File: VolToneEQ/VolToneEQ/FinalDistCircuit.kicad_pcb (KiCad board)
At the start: 4 copper layers, 96.8 x 83.6 mm, 93 parts, among them Q1 ZTX951, Q2 ZTX951, U1 TL072, U2 TL072, U3 TL072, U4 TL072

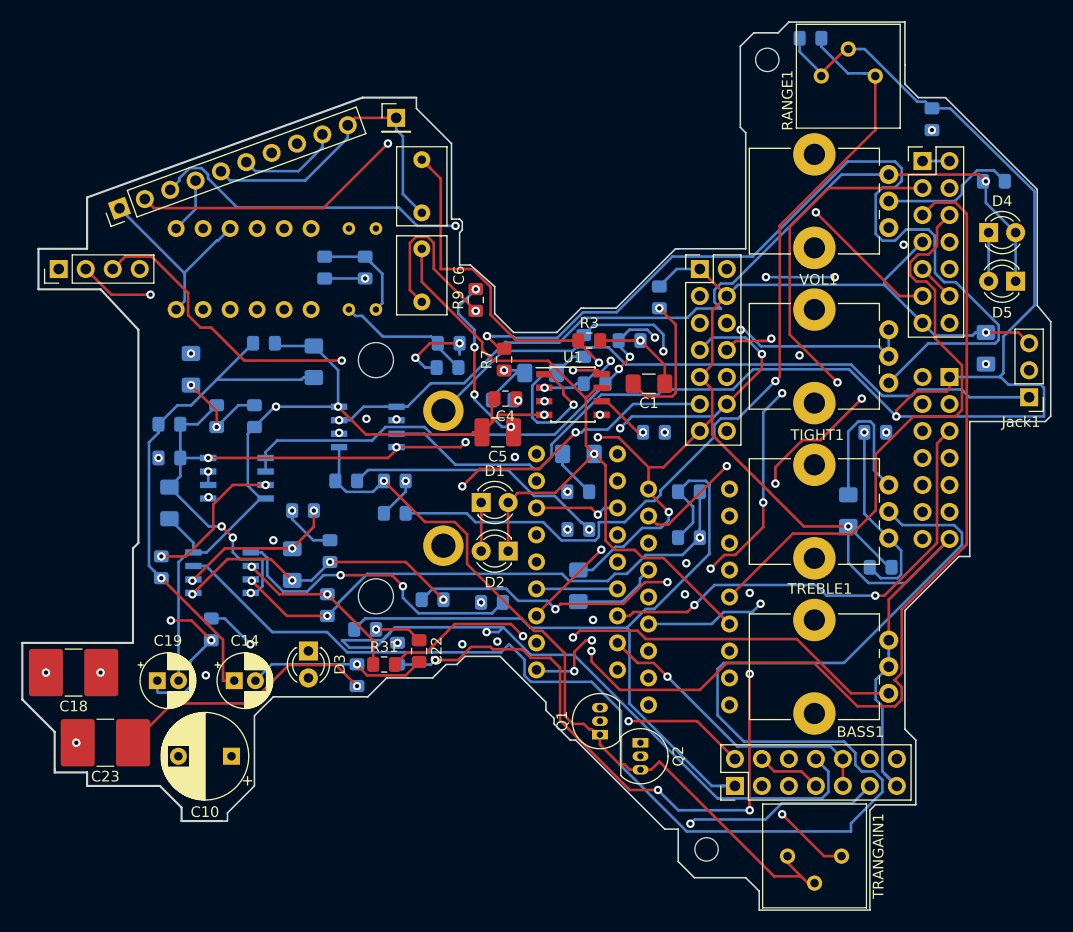
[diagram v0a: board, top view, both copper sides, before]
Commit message: added 100k parallel to volume
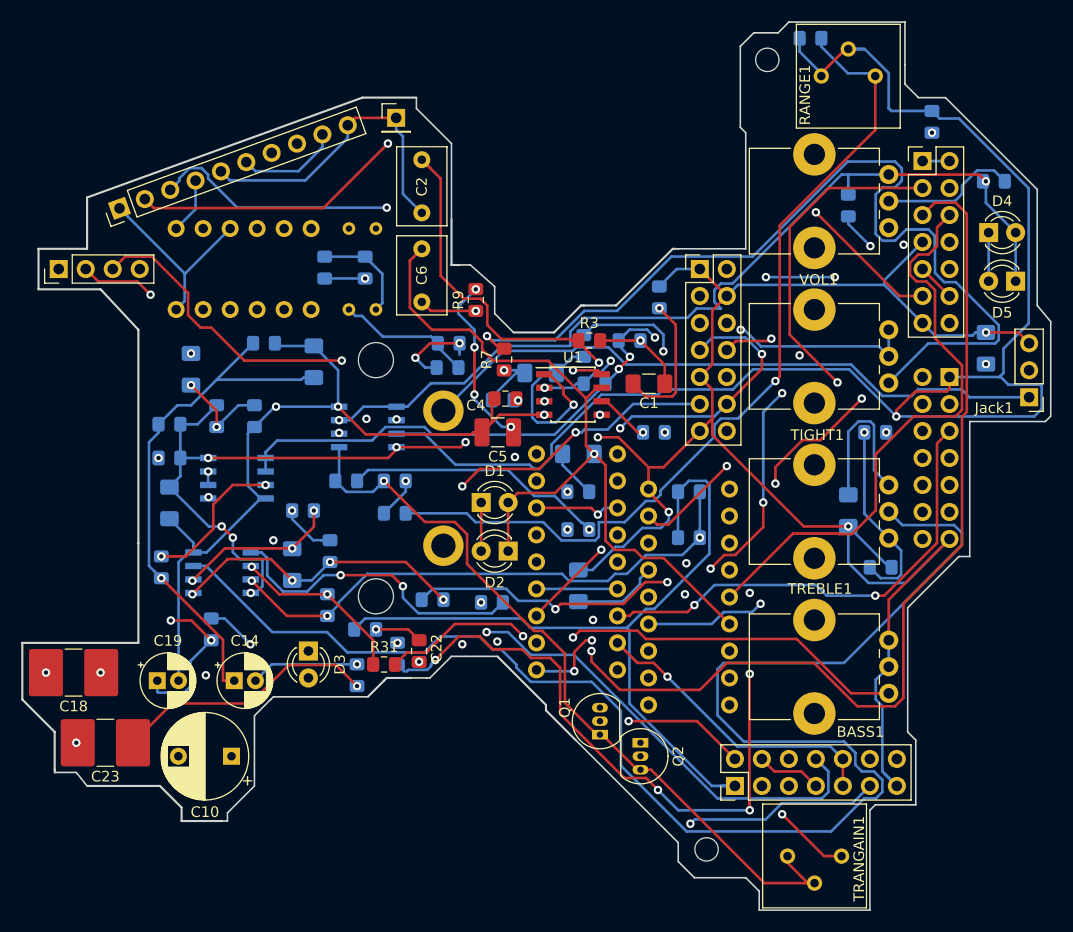
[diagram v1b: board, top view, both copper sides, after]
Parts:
- added R36: 100k, Resistor_SMD:R_0805_2012Metric_Pad1.15x1.40mm_HandSolder, B.Cu at (121.9, 122.9)
- VOL1: value 50k -> 100k
- moved R35 0.24 mm to (129.8, 115.1)
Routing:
- net NRED2: track 102.7 -> 81.3 mm
- net OUT: track 154.9 -> 140.2 mm
- net Net-(C6-Pad2): track 42.9 -> 33.0 mm
- net Net-(R27-Pad1): track 69.4 -> 73.1 mm, vias 5 -> 6
- net GAINSTAGEPOTIN: track 69.0 -> 72.0 mm
- net Vref2: track 98.8 -> 101.4 mm
- net PRESIN: track 137.8 -> 140.0 mm
- net BRBLACK: track 101.7 -> 103.7 mm
- net ODMIDGND: track 74.4 -> 73.2 mm
- net ODout: track 69.1 -> 70.1 mm
- net NGRN2: track 94.4 -> 95.4 mm
- net BRGRN2: track 345.3 -> 346.3 mm, vias 9 -> 10
- net Net-(4pdt1-Pad6): track 8.28 -> 7.62 mm
- net NGRN: track 24.6 -> 23.9 mm
- net BTONEIN: track 93.7 -> 93.1 mm
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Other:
- outline, holes or cut-outs redrawn

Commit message: improved some traces
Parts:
- renumbered BASS1 to BASS, TIGHT1 to TIGHT, TREBLE1 to TREBLE, VOL1 to VOL
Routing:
- net OUT: track 140.2 -> 75.1 mm, vias 1 -> 2
- net Net-(TREBLE1-Pad2): track 142.0 -> 119.1 mm
- net PRESIN: track 140.0 -> 119.6 mm
- net NOUT: track 119.3 -> 99.7 mm
- net Net-(C16-Pad1): track 15.1 -> 4.19 mm, vias 0 -> 1
- net Net-(R7-Pad2): track 91.0 -> 86.3 mm
- net BRTONEGANG1IN: track 55.3 -> 51.1 mm
- net BRGRN: track 19.1 -> 15.0 mm
- net NVINTRAD: track 69.8 -> 65.8 mm
- net Vref2: track 101.4 -> 98.2 mm
- net BRRED2: track 101.5 -> 99.2 mm
- net NVOUTTRAD: track 84.3 -> 86.1 mm
- net GAINPOTOUT: track 68.7 -> 70.4 mm
- net GAINSTAGEPOTIN: track 72.0 -> 71.5 mm
- net Net-(C5-Pad1): track 16.4 -> 15.8 mm
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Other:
- outline, holes or cut-outs redrawn
- board text added: "OFF"
- board text added: "ON"
- board text added: "PUPS PHASE"
- board text added: "TRBLD"

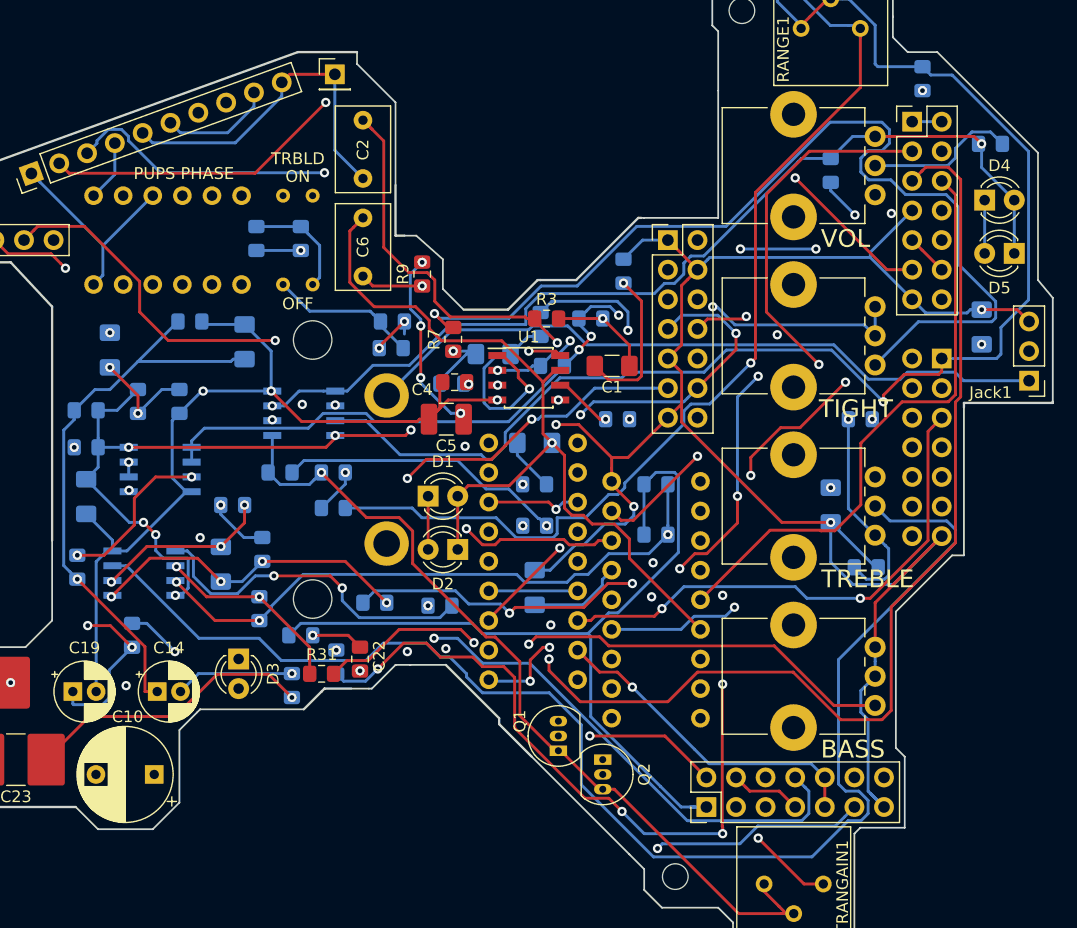
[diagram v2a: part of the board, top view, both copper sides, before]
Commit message: changed potbreakout and widened traces
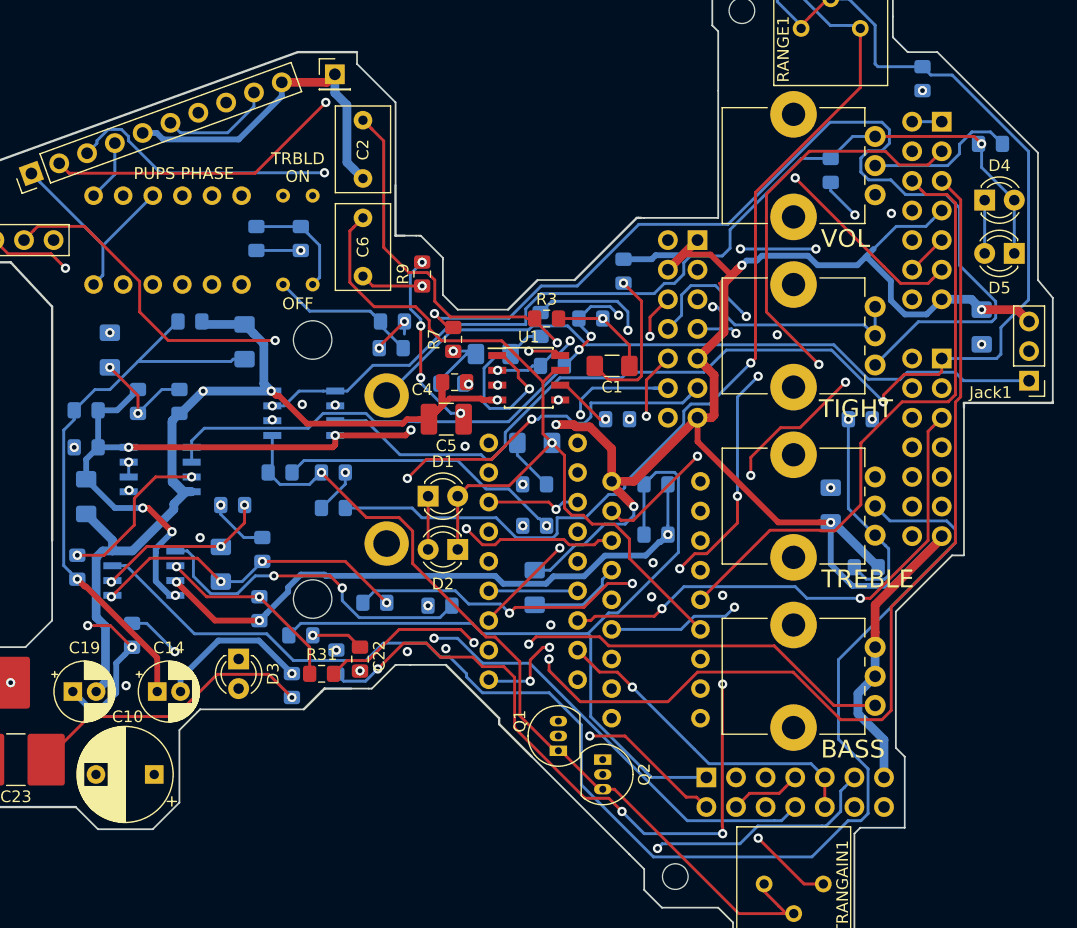
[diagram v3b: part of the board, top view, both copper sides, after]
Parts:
- BridgeTonePot1, BridgeVolPot1, NeckVolumePot1: moved to B.Cu
- moved BridgeTonePot1 2.54 mm to (131.4, 118.7), turned to 180 degrees
- moved BridgeVolPot1 2.54 mm to (110.5, 128.9), turned to 180 degrees
- moved NeckVolumePot1 2.54 mm to (111.3, 175.0), turned to 270 degrees
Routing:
- net BRGRN2: track 346.3 -> 386.3 mm, vias 10 -> 11
- net NVOUTTRAD: track 86.1 -> 108.3 mm
- net Net-(BridgeVolPot1-Pad8): track 68.9 -> 78.0 mm
- net BVINTRAD: track 67.8 -> 61.6 mm, vias 0 -> 1
- net BROUT: track 72.8 -> 77.8 mm
- net BTONEIN: track 93.1 -> 88.6 mm
- net NRED2: track 80.7 -> 76.2 mm
- net NBLACK: track 123.9 -> 127.9 mm
- net ODin: track 47.0 -> 43.5 mm
- net BRWHT: track 90.4 -> 93.9 mm
- net BRTONEGANG2IN: track 65.8 -> 69.3 mm
- net BRBLACK: track 103.7 -> 100.4 mm
- net Net-(9V1-Pad1): track 18.6 -> 21.3 mm
- net ODMIDIN: track 102.3 -> 99.8 mm
- net ODMIDGND: track 73.2 -> 70.8 mm
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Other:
- outline, holes or cut-outs redrawn
- net class Power added: clearance 0.2, trace_width 0.75, via_dia 0.8, via_drill 0.4
- net class Power2 added: clearance 0.2, trace_width 0.5, via_dia 0.8, via_drill 0.4

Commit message: finalized and ordered all boards
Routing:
- net BRGRN2: track 386.3 -> 388.4 mm
- net Net-(R13-Pad1): track 73.3 -> 72.6 mm
- net BVINTRAD: track 61.6 -> 61.0 mm
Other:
- outline, holes or cut-outs redrawn

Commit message: fucked it up. gotta redo
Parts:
- moved D2 195.0 mm to (248.4, 41.8)
- moved D1 189.9 mm to (245.9, 46.4)
- moved C2 186.8 mm to (244.7, 27.2)
- moved C6 186.5 mm to (239.3, 27.2)
- moved REF** 157.0 mm to (249.8, 29.8)
- moved REF** 155.7 mm to (241.2, 102.0)
- moved NeckTonePot1 149.4 mm to (242.3, 38.9)
- moved Q2 146.3 mm to (226.2, 95.5), turned to 90 degrees
- moved 6pdt1 143.7 mm to (207.0, 84.1)
- moved TRANGAIN1 143.5 mm to (231.3, 98.4)
- moved C19 143.4 mm to (178.2, 91.2)
- moved 4pdt1 142.6 mm to (200.4, 47.8)
- moved 9V1 140.8 mm to (146.8, 71.9)
- moved Jack1 138.0 mm to (249.9, 58.9)
- moved C23 137.9 mm to (163.0, 91.7)
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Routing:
- net BRGRN2: track 388.4 -> 0.00 mm, vias 11 -> 0
- net NBLACK: track 127.9 -> 0.00 mm
- net PRESIN: track 119.6 -> 0.00 mm, vias 1 -> 0
- net Net-(TREBLE1-Pad2): track 118.3 -> 0.00 mm
- net NVOUTTRAD: track 108.3 -> 0.00 mm
- net BRBLACK: track 100.4 -> 0.00 mm, vias 2 -> 0
- net ODMIDIN: track 99.8 -> 0.00 mm, vias 4 -> 0
- net BRRED2: track 99.2 -> 0.00 mm, vias 3 -> 0
- net Vref2: track 99.1 -> 0.00 mm, vias 3 -> 0
- net NOUT: track 98.6 -> 0.00 mm, vias 3 -> 0
- net NGRN2: track 97.5 -> 0.00 mm, vias 2 -> 0
- net BRWHT: track 93.9 -> 0.00 mm, vias 2 -> 0
- net Net-(C10-Pad1): track 88.9 -> 0.00 mm, vias 8 -> 0
- net BTONEIN: track 88.6 -> 0.00 mm, vias 1 -> 0
- net Net-(BASS1-Pad3): track 86.9 -> 0.00 mm, vias 3 -> 0
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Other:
- board size 96.8 x 83.6 mm -> 101.3 x 79.2 mm

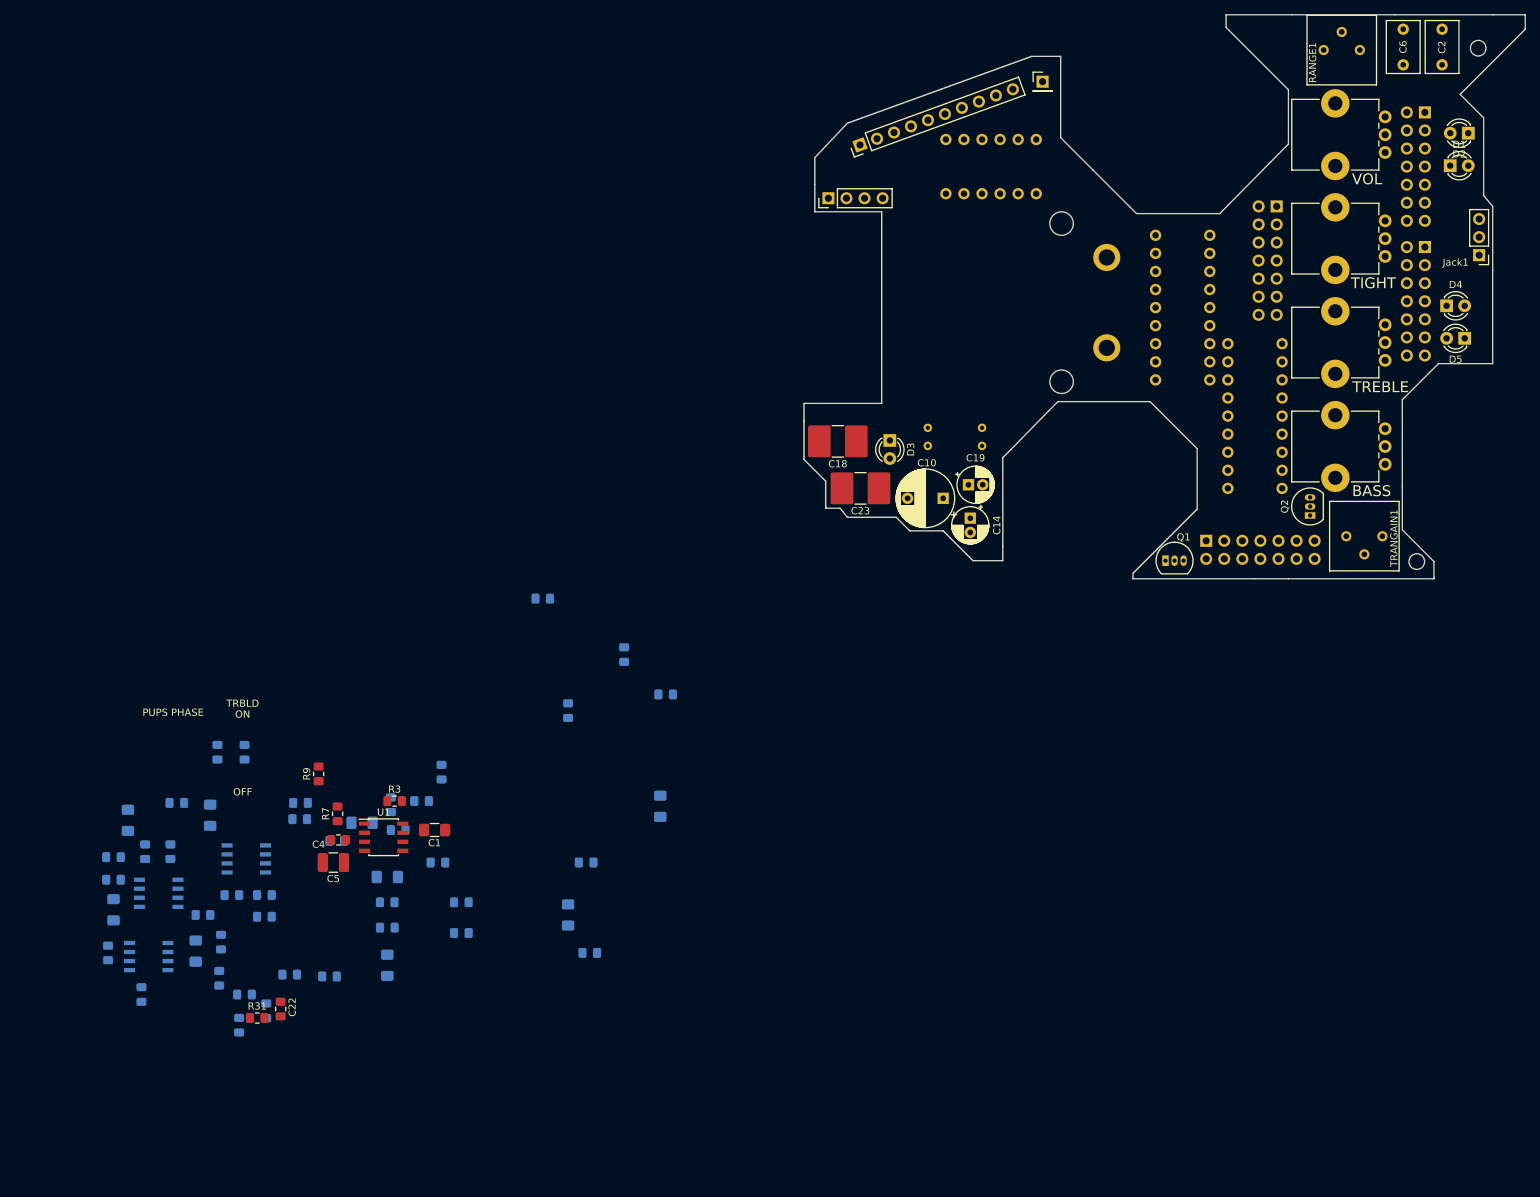
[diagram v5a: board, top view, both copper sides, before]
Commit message: revised layout to fit
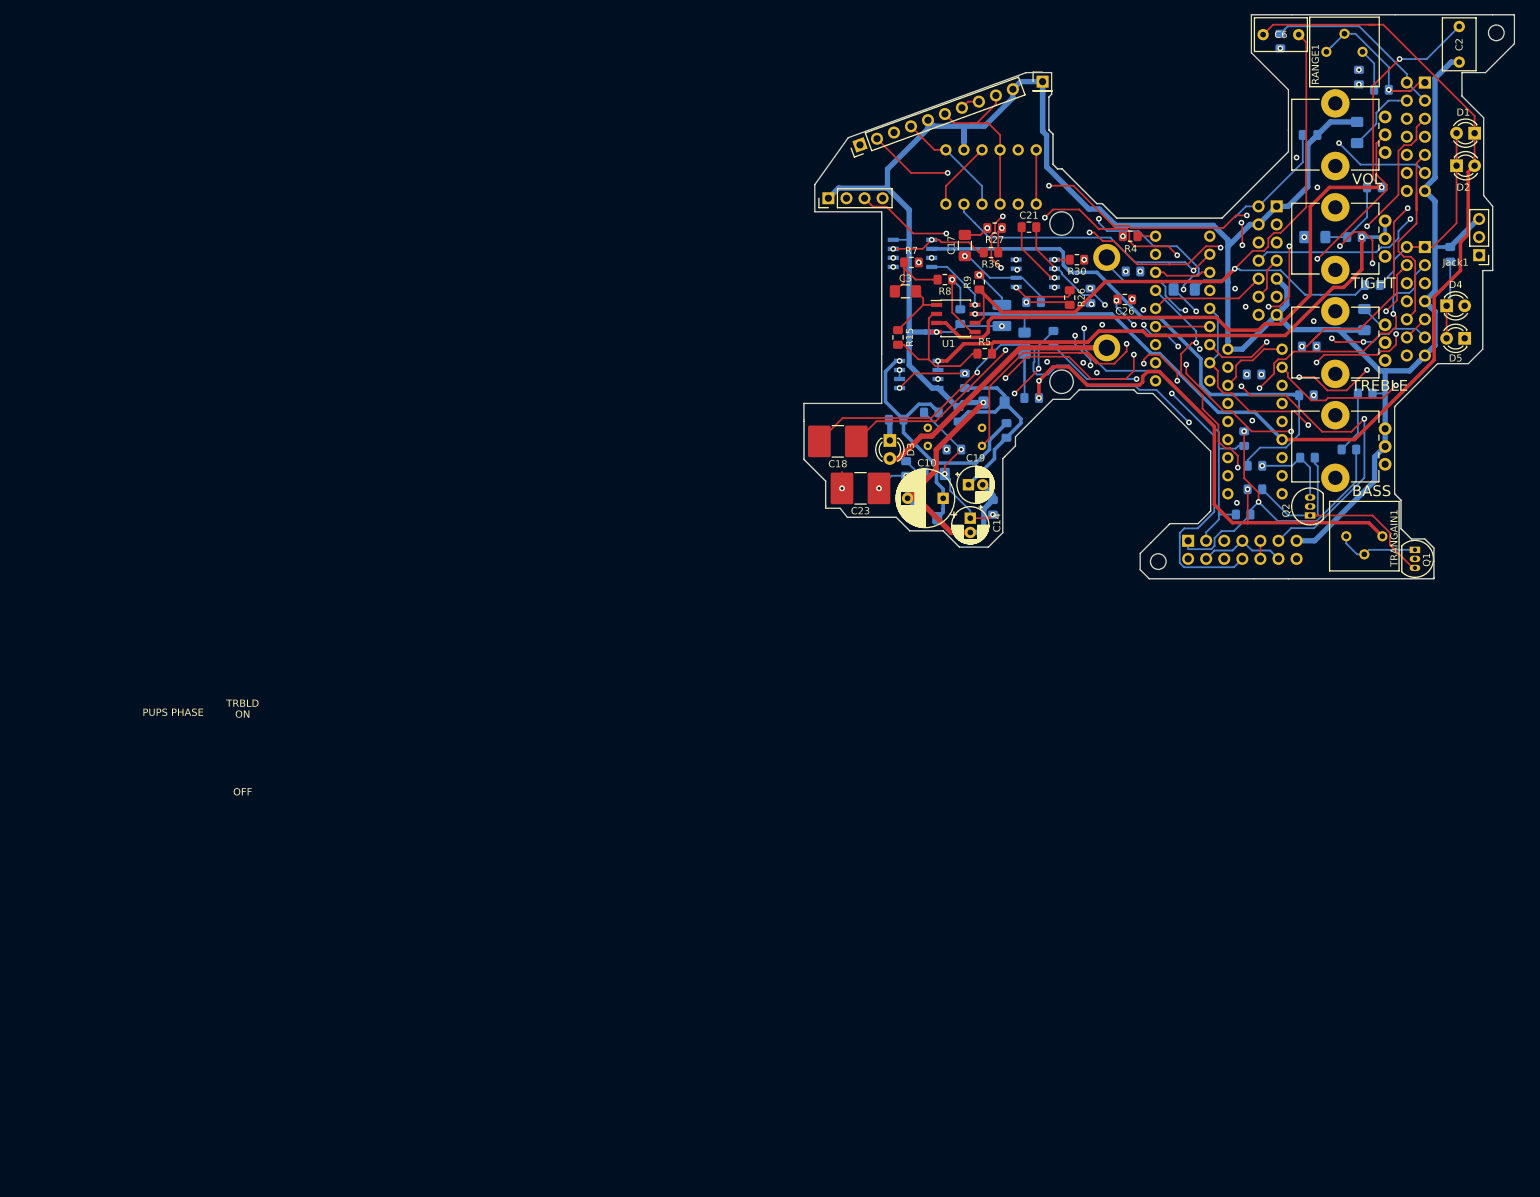
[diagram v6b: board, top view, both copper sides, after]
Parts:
- C1, C22, C4, C5, R3, R31: moved to B.Cu
- C17, C21, C26, C3, R15, R26, R27, R30, R36, R4, R5, R8: moved to F.Cu
- moved C22 175.2 mm to (233.9, 78.4), turned to 0 degrees
- moved R32 173.1 mm to (231.6, 86.2), turned to 180 degrees
- moved R31 166.7 mm to (218.3, 75.7)
- moved R18 163.7 mm to (225.7, 78.6)
- moved C8 163.2 mm to (225.8, 87.4)
- moved R3 162.4 mm to (235.2, 49.4), turned to 180 degrees
- moved U3 157.3 mm to (187.6, 61.5)
- moved C13 155.7 mm to (245.9, 58.8), turned to 90 degrees
- moved C21 155.2 mm to (186.7, 55.0), turned to 0 degrees
- moved R10 154.4 mm to (234.9, 63.1)
- moved R2 153.2 mm to (232.4, 56.4), turned to 180 degrees
- moved R17 151.7 mm to (218.4, 88.5), turned to 0 degrees
- moved R1 151.4 mm to (226.2, 42.0), turned to 0 degrees
- moved R26 149.7 mm to (192.4, 64.9), turned to 270 degrees
- moved C1 149.1 mm to (226.9, 56.4)
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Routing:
- net BRGRN2: track 0.00 -> 390.2 mm, vias 0 -> 4
- net Vref2: track 0.00 -> 157.5 mm, vias 0 -> 4
- net GAINSTAGEPOTIN: track 0.00 -> 152.2 mm, vias 0 -> 1
- net ODMIDIN: track 0.00 -> 117.9 mm, vias 0 -> 3
- net BRRED2: track 0.00 -> 113.4 mm, vias 0 -> 2
- net Net-(C2-Pad1): track 0.00 -> 112.4 mm, vias 0 -> 2
- net PRESIN: track 0.00 -> 111.8 mm, vias 0 -> 3
- net Vref: track 0.00 -> 109.2 mm, vias 0 -> 2
- net NGRN2: track 0.00 -> 106.4 mm, vias 0 -> 6
- net Net-(C6-Pad2): track 0.00 -> 104.8 mm, vias 0 -> 1
- net Net-(R13-Pad1): track 0.00 -> 104.7 mm, vias 0 -> 4
- net BRBLACK: track 0.00 -> 102.8 mm, vias 0 -> 4
- net Net-(BASS1-Pad3): track 0.00 -> 100.2 mm, vias 0 -> 2
- net BRWHT: track 0.00 -> 98.3 mm, vias 0 -> 4
- net Net-(C8-Pad1): track 0.00 -> 97.9 mm, vias 0 -> 2
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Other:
- board size 101.3 x 79.2 mm -> 99.8 x 79.2 mm
